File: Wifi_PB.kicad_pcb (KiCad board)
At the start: 2 copper layers, 100 x 50 mm, 162 parts, among them P1 CONN_01X02, P10 CONN_01X01, P13 CONN_01X04, P14 CONN_01X04, P15 USB_MINI, P16 CONN_01X01, P17 CONN_01X01, P18 CONN_01X01, P19 CONN_01X01, P2 CONN_01X03, P3 CONN_01X03, P4 CONN_01X03, P5 CONN_01X03, P6 CONN_01X01, P7 CONN_01X01, P8 CONN_01X01, P9 CONN_01X01, Q1 SMBT3904, Q10 BC849, Q11 NX2301P, Q2 SMBT3904, Q3 BSS138, Q4 BSS138, Q5 SMBT3904, Q6 SMBT3904, Q7 SMBT3904, Q8 SMBT3904, Q9 SMBT3904, SW1 Pulsador_2p, SW2 Pulsador_2p, SW3 Pulsador_2p, SW4 Pulsador_2p, U1 MCP73831T, U10 Matriz_5x7_Anodo_Filas, U11 40106, U12 MCP1640, U2 LD1117S33TR, U3 CH340T, U4 ESP8266, U5 MMA7660FC, U6 MCP23017, U7 MCP23017, U8 MCP3204, U9 PCA9551, Y1 12MHz

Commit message: cambiar ch340T por ch340g y añadir nc a pines
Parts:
- added P12: CONN_01X04, Socket_Strips:Socket_Strip_Straight_1x04_Pitch2.54mm, F.Cu at (151.0, 59.5)
- added REF**: MountingHole_3.2mm_M3_DIN965_Pad, Mounting_Holes:MountingHole_3.2mm_M3_DIN965_Pad, F.Cu at (152.0, 85.0)
- added REF**: MountingHole_3.2mm_M3_DIN965_Pad, Mounting_Holes:MountingHole_3.2mm_M3_DIN965_Pad, F.Cu at (152.0, 41.0)
- added REF**: MountingHole_3.2mm_M3_DIN965_Pad, Mounting_Holes:MountingHole_3.2mm_M3_DIN965_Pad, F.Cu at (58.0, 41.0)
- added REF**: MountingHole_3.2mm_M3_DIN965_Pad, Mounting_Holes:MountingHole_3.2mm_M3_DIN965_Pad, F.Cu at (58.0, 85.0)
- R21, R26, R27, R28, R31, R32, R33, U5, U8, U9: moved to B.Cu
- U3: value CH340T -> CH340G; footprint Housings_SSOP:SSOP-20_4.4x6.5mm_Pitch0.65mm -> Housings_SOIC:SOIC-16_3.9x9.9mm_Pitch1.27mm
- moved U9 219.0 mm to (127.0, 64.0), turned to 180 degrees
- moved U8 211.2 mm to (127.0, 74.0), turned to 180 degrees
- moved R28 149.7 mm to (99.0, 64.0), turned to 180 degrees
- moved R27 142.5 mm to (99.0, 60.0), turned to 180 degrees
- moved U5 138.7 mm to (109.0, 73.0), turned to 180 degrees
- moved R21 138.5 mm to (99.0, 66.0), turned to 180 degrees
- moved R26 137.6 mm to (99.0, 56.0), turned to 180 degrees
- moved R33 135.1 mm to (99.0, 62.0), turned to 180 degrees
- moved R31 132.2 mm to (99.0, 54.0), turned to 180 degrees
- moved R32 127.8 mm to (99.0, 58.0), turned to 180 degrees
- moved U6 9.00 mm to (90.0, 60.0)
- moved U7 9.00 mm to (90.0, 73.0)
- moved P13 3.68 mm to (151.0, 71.5)
- moved U3 2.49 mm to (71.0, 51.0)
- moved P14 1.10 mm to (151.0, 46.5)
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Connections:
- C18 pad 2: GNDA -> GND
- R39 pad 2: PB3 -> PB7
- R40 pad 2: PB2 -> PB6
- R41 pad 2: PB1 -> PB5
- R42 pad 2: PB0 -> PB4
- RV1 pad 2: A7 -> CH0
- SW1 pad 2: PB2 -> PB6
- SW2 pad 2: PB3 -> PB7
- SW3 pad 2: PB0 -> PB4
- SW4 pad 2: PB1 -> PB5
- U11 pad 14: VDD -> +5V
- U11 pad 7: VSS -> GND
- U3 pad 1: Net-(U3-Pad1) -> GND
- U3 pad 10: Net-(C6-Pad1) -> Net-(U3-Pad10)
- U3 pad 13: Net-(U3-Pad13) -> Net-(Q2-Pad2)
- U3 pad 14: Net-(U3-Pad14) -> Net-(Q1-Pad2)
- U3 pad 15: Net-(Q2-Pad2) -> Net-(U3-Pad15)
- U3 pad 16: Net-(Q1-Pad2) -> +5V
- U3 pad 2: Net-(U3-Pad2) -> Net-(R9-Pad2)
- U3 pad 3: Net-(R9-Pad2) -> Net-(R8-Pad2)
- U3 pad 4: Net-(R8-Pad2) -> Net-(C9-Pad1)
- U3 pad 5: Net-(C9-Pad1) -> /Control/USBD+
- U3 pad 6: /Control/USBD+ -> /Control/USBD-
- U3 pad 7: /Control/USBD- -> Net-(C5-Pad1)
- U3 pad 8: GND -> Net-(C6-Pad1)
- U3 pad 9: Net-(C5-Pad1) -> Net-(U3-Pad9)
- U8 pad 11: CLK -> SCK
- U8 pad 12: GNDA -> GND
- U9 pad 14: A5 -> SCL
- U9 pad 15: A4 -> SDA
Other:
- net class Default: clearance 0.2 -> 0.2032; trace_width 0.25 -> 0.1524; via_dia 0.8 -> 0.6; via_drill 0.4 -> 0.3
- net class power added: clearance 0.254, trace_width 0.254, via_dia 0.8, via_drill 0.4
- rule trace_clearance: 0.2 -> 0.2032
- rule trace_min: 0.2 -> 0.1524

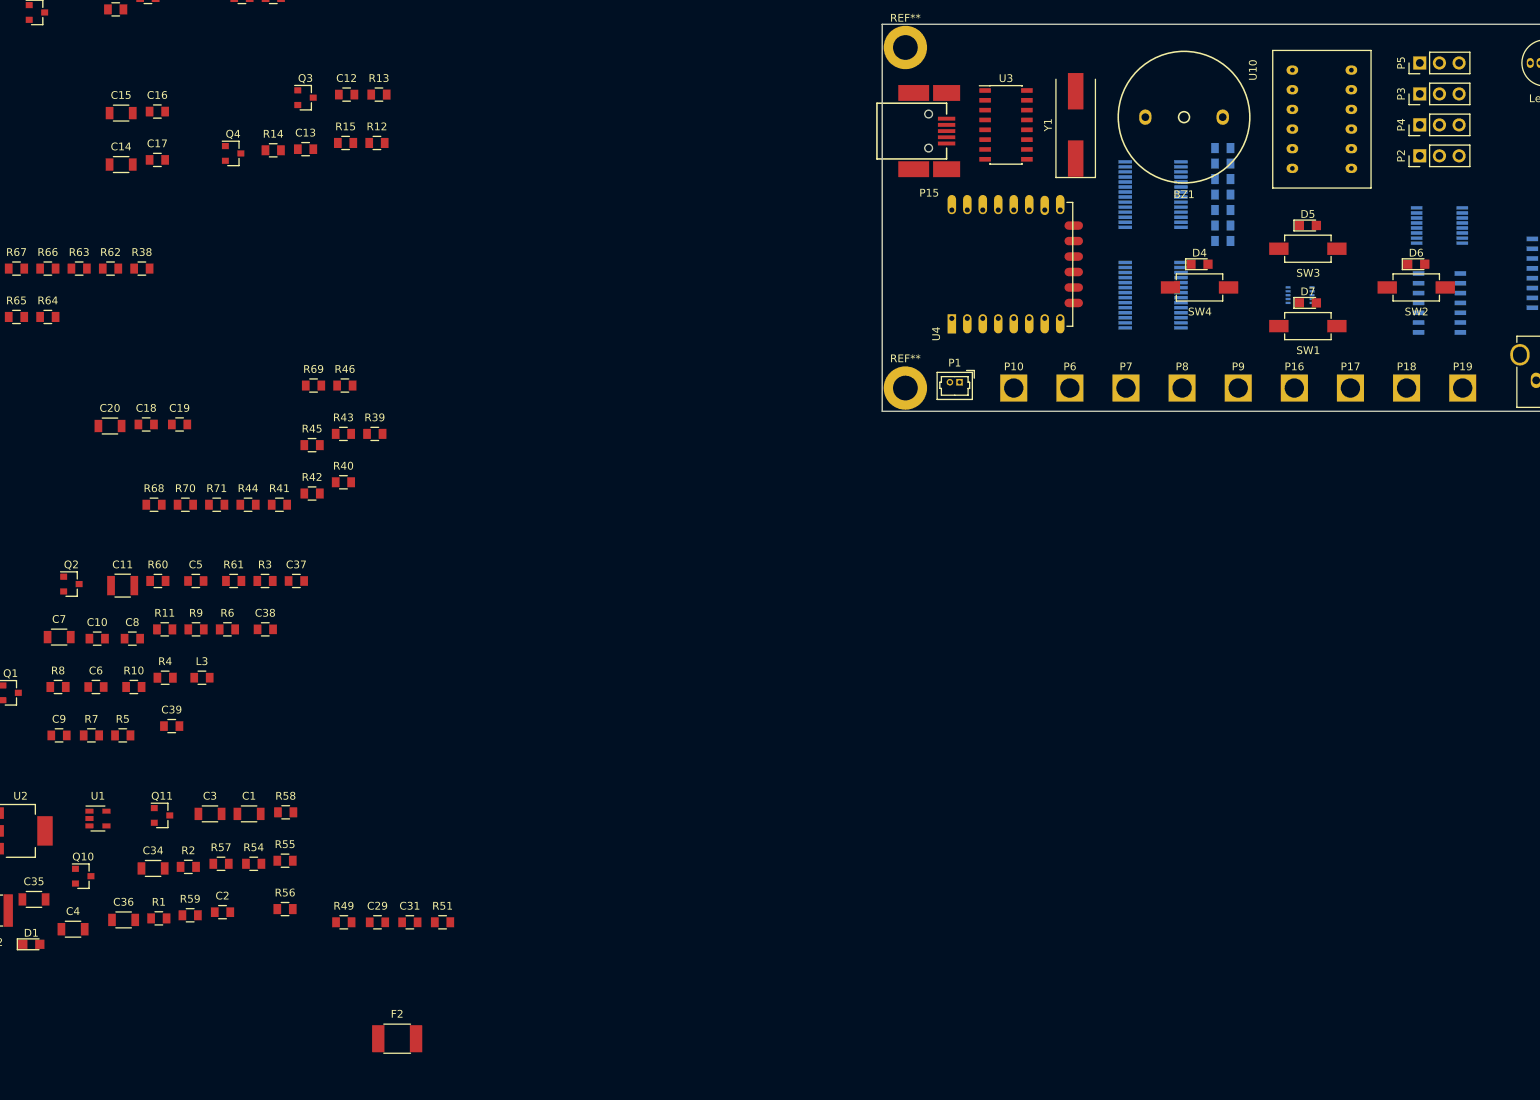
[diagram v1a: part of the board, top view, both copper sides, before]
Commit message: cambiado cristal de cuarzo por resonador
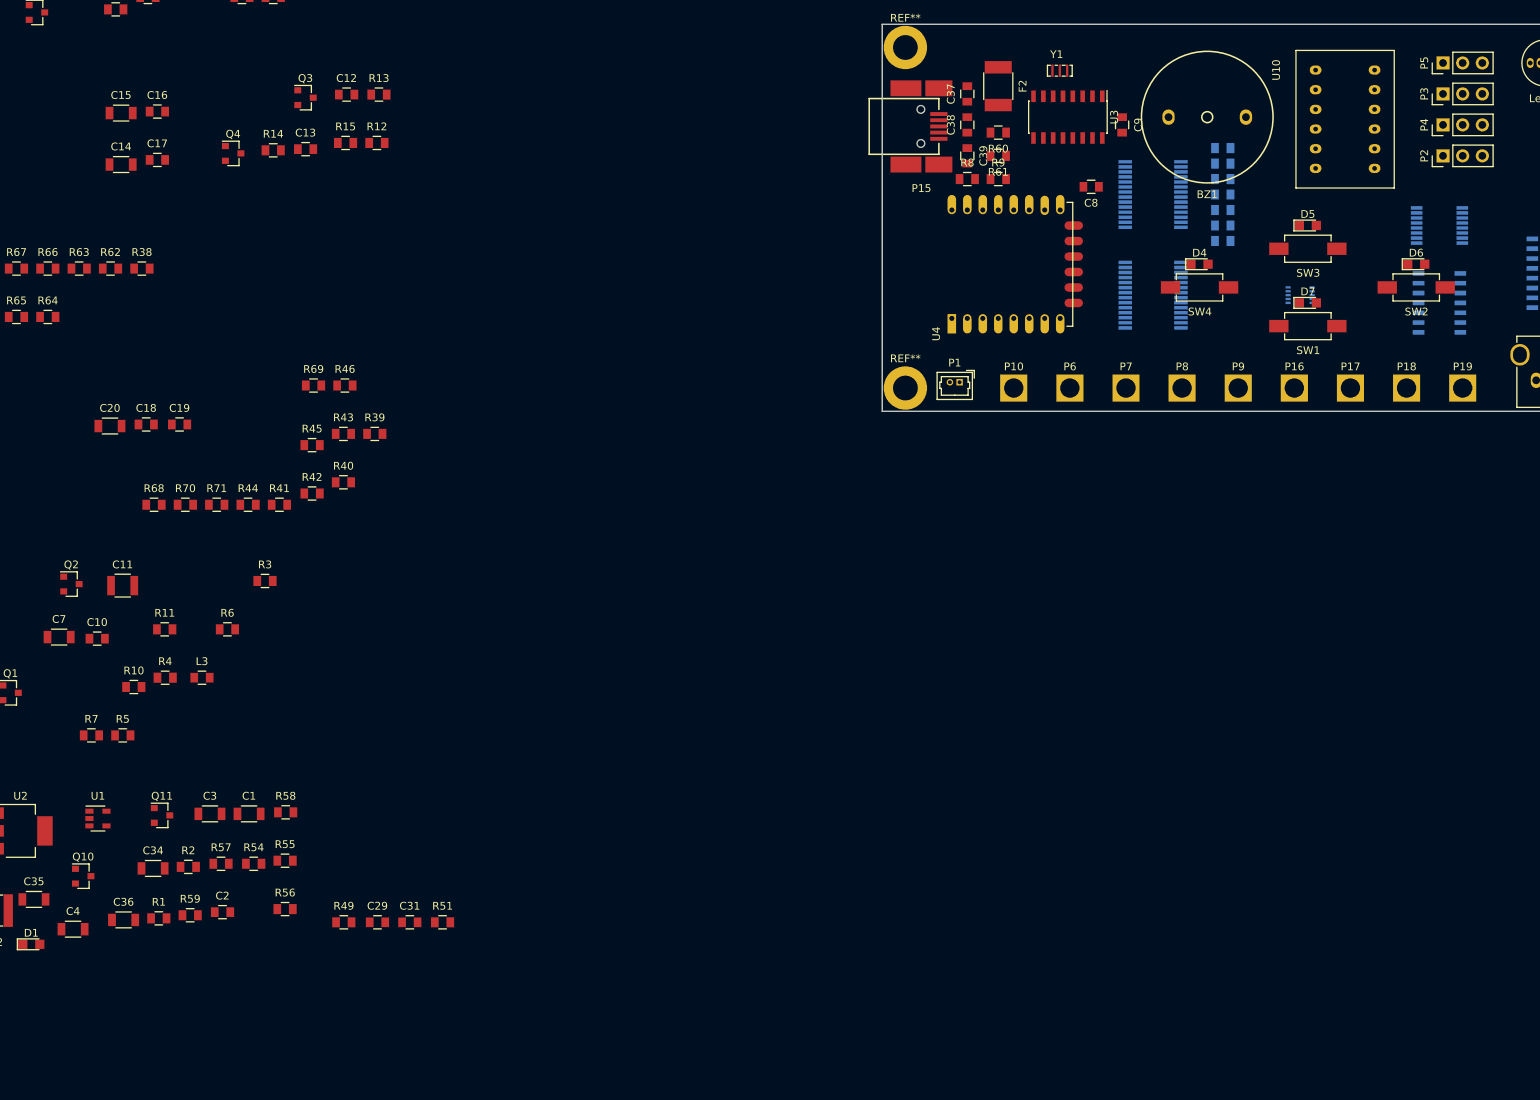
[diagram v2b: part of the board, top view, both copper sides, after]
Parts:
- removed C5, C6: 0,022n, Capacitors_SMD:C_0805
- Y1: value 12MHz -> Cristal; footprint Cristal:Cristal_SMD_HC49-SD -> Cristal:Murata_CSTCE_V_A
- moved C9 158.4 mm to (86.0, 51.0), turned to 270 degrees
- moved F2 145.5 mm to (70.0, 46.0), turned to 270 degrees
- moved C8 136.9 mm to (82.0, 59.0), turned to 180 degrees
- moved R8 134.6 mm to (66.0, 58.0)
- moved C39 126.5 mm to (66.0, 55.0), turned to 270 degrees
- moved R60 123.1 mm to (70.0, 52.0), turned to 180 degrees
- moved R9 118.9 mm to (70.0, 58.0)
- moved R61 113.0 mm to (70.0, 55.0), turned to 180 degrees
- moved C38 111.7 mm to (66.0, 51.0), turned to 90 degrees
- moved C37 107.1 mm to (66.0, 47.0), turned to 90 degrees
- moved U3 8.06 mm to (79.0, 50.0), turned to 270 degrees
- moved Y1 7.29 mm to (78.0, 44.0), turned to 180 degrees
- moved BZ1 3.00 mm to (97.0, 50.0)
- moved P2 3.00 mm to (127.5, 55.0)
- moved P3 3.00 mm to (127.5, 47.0)
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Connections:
- C7 pad 1: +5V -> VUSB
- C9 pad 1: Net-(C9-Pad1) -> +3V3
- F2 pad 2: Net-(F2-Pad2) -> Net-(C37-Pad1)
- U3 pad 4: Net-(C9-Pad1) -> +3V3
- U3 pad 8: Net-(C6-Pad1) -> Net-(U3-Pad8)
- Y1 pad 2: Net-(C6-Pad1) -> GND

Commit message: place inicial sobre la pcb
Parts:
- removed L3: Ferrita, Capacitors_SMD:C_0805
- C1, C12, C13, C14, C15, C16, C17, C18, C19, C2, C20, C21, C22, C23, C24, C25, C29, C3, C30, C31, C32, C33, C34, C35, C36, C4, C7, D3, L2, Q10, Q11, Q3, Q4, Q5, Q6, Q7, Q8, Q9, R1, R12, R13, R14, R15, R16, R17, R18, R19, R2, R20, R22, R23, R24, R25, R29, R30, R34, R35, R36, R37, R38, R39, R40, R41, R42, R43, R44, R45, R46, R49, R50, R51, R52, R53, R54, R55, R56, R57, R58, R59, R62, R63, R64, R65, R66, R67, R68, R69, R70, R71, U1, U12, U2: moved to B.Cu
- moved R52 247.1 mm to (146.0, 52.0), turned to 180 degrees
- moved C33 236.0 mm to (146.0, 50.0), turned to 180 degrees
- moved C30 233.7 mm to (140.0, 53.0), turned to 180 degrees
- moved C32 231.7 mm to (146.0, 46.0), turned to 180 degrees
- moved R50 227.6 mm to (146.0, 74.0), turned to 180 degrees
- moved C23 210.0 mm to (134.0, 44.0), turned to 180 degrees
- moved R16 206.9 mm to (133.0, 57.0), turned to 180 degrees
- moved C24 206.2 mm to (134.0, 48.0), turned to 180 degrees
- moved R17 206.0 mm to (122.0, 40.0)
- moved R20 202.7 mm to (122.0, 52.0)
- moved R65 201.1 mm to (142.0, 46.0), turned to 270 degrees
- moved C25 198.9 mm to (134.0, 52.0), turned to 180 degrees
- moved C21 198.8 mm to (129.0, 57.0)
- moved C22 198.6 mm to (134.0, 40.0), turned to 180 degrees
- moved R67 198.3 mm to (140.0, 46.0), turned to 270 degrees
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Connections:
- D4 pad 1: Net-(D4-Pad1) -> GND
- D4 pad 2: PC0 -> Net-(D4-Pad2)
- D5 pad 1: Net-(D5-Pad1) -> GND
- D5 pad 2: PC1 -> Net-(D5-Pad2)
- D6 pad 1: Net-(D6-Pad1) -> GND
- D6 pad 2: PC2 -> Net-(D6-Pad2)
- D7 pad 1: Net-(D7-Pad1) -> GND
- D7 pad 2: PC3 -> Net-(D7-Pad2)
- R38 pad 1: Net-(D6-Pad1) -> PC2
- R38 pad 2: GND -> Net-(D6-Pad2)
- R62 pad 1: Net-(D4-Pad1) -> PC0
- R62 pad 2: GND -> Net-(D4-Pad2)
- R63 pad 1: Net-(D5-Pad1) -> PC1
- R63 pad 2: GND -> Net-(D5-Pad2)
- R64 pad 1: Net-(D7-Pad1) -> PC3
- R64 pad 2: GND -> Net-(D7-Pad2)
- U1 pad 2: Net-(R2-Pad1) -> GND
- U1 pad 5: (no net) -> Net-(R2-Pad1)
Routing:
- added copper zone on B.Cu, net GND
- added copper zone on F.Cu, net GND

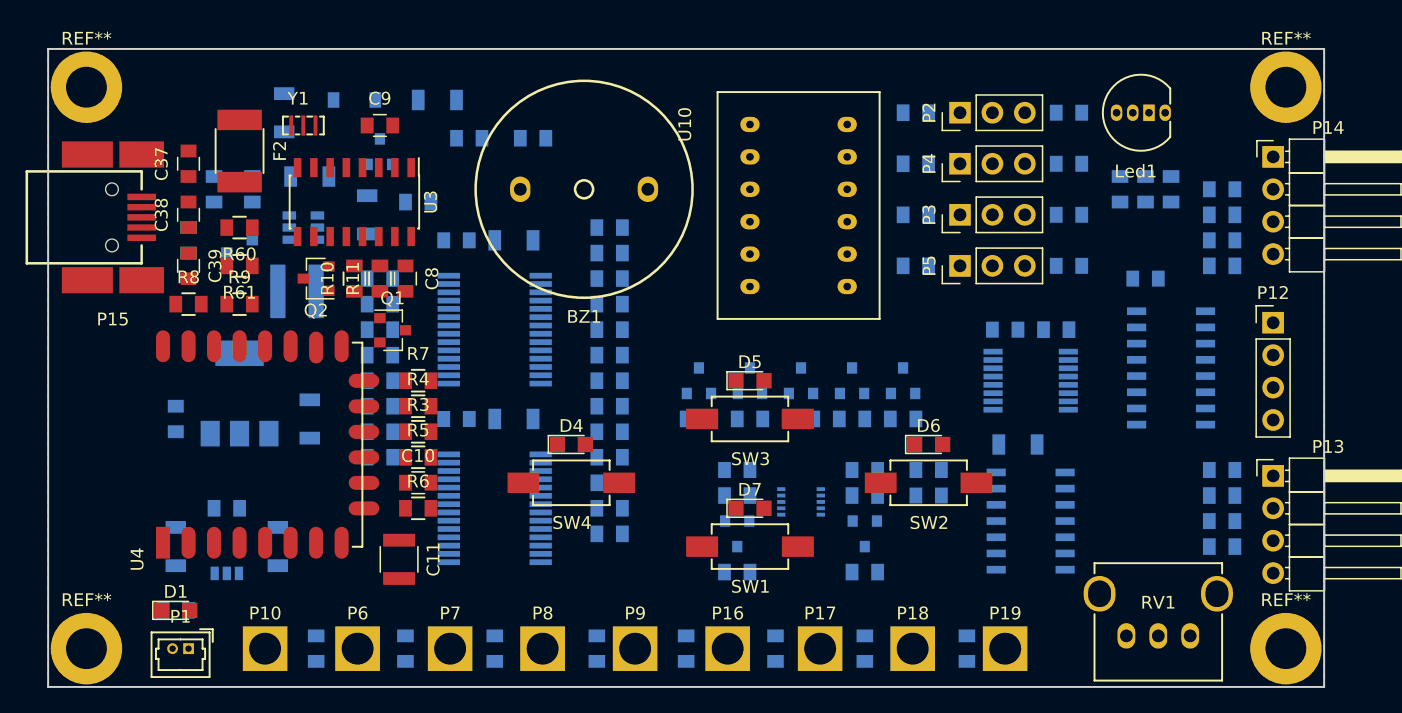
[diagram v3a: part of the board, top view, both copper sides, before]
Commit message: ordenar componentes y referencias
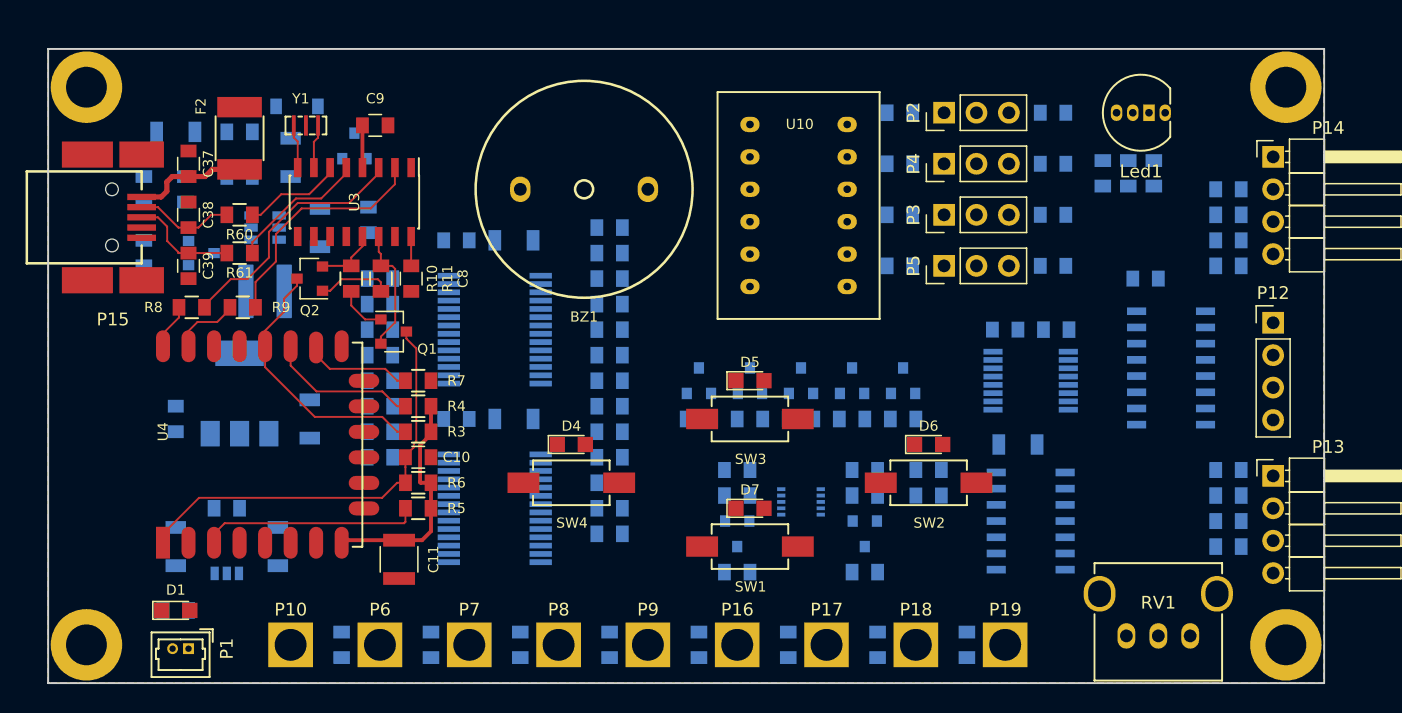
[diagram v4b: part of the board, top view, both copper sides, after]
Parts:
- removed C36: 4u7, Capacitors_SMD:C_1206
- moved R58 23.0 mm to (69.0, 41.5)
- moved R57 18.2 mm to (69.0, 45.0), turned to 180 degrees
- moved C7 8.63 mm to (64.0, 41.5), turned to 0 degrees
- moved R54 5.50 mm to (61.5, 46.0)
- moved R56 5.25 mm to (64.8, 46.0)
- moved D3 4.53 mm to (73.5, 39.5)
- moved R59 4.14 mm to (79.1, 48.4), turned to 90 degrees
- moved R5 4.00 mm to (83.0, 71.0)
- moved C34 3.83 mm to (75.3, 49.0)
- moved R55 3.64 mm to (61.5, 51.0)
- moved Q10 3.16 mm to (66.0, 51.0)
- moved U12 3.00 mm to (71.0, 49.0)
- moved L2 2.50 mm to (71.0, 54.0)
- moved C35 2.12 mm to (73.0, 43.5), turned to 90 degrees
- moved Q11 2.05 mm to (78.0, 42.6)
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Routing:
- net /Control/~RST: track 0.00 -> 33.2 mm
- net +3V3: track 0.00 -> 21.8 mm
- net /Control/GPIO0: track 0.00 -> 21.1 mm
- net Net-(R8-Pad2): track 0.00 -> 19.7 mm
- net Net-(R9-Pad2): track 0.00 -> 18.7 mm
- net /Control/EN: track 0.00 -> 16.1 mm
- net /Control/GPIO2: track 0.00 -> 11.1 mm
- net /Control/USBD+: track 0.00 -> 10.9 mm
- net Net-(Q1-Pad2): track 0.00 -> 9.92 mm
- net Net-(C37-Pad1): track 0.00 -> 9.00 mm
- net Net-(C39-Pad1): track 0.00 -> 8.53 mm
- net /Control/USBD-: track 0.00 -> 7.89 mm
- net /Control/GPIO15: track 0.00 -> 7.83 mm
- net Net-(C38-Pad1): track 0.00 -> 7.75 mm
- net /Control/RxD: track 0.00 -> 6.00 mm
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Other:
- board size 100 x 50 mm -> 100 x 49.7 mm
